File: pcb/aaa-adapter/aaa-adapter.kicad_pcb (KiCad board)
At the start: 2 copper layers, 127 x 47 mm, 3 parts

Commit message: Unchecked
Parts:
- removed REF** (x3): PinSocket_1x01_P2.54mm_Vertical, Connector_PinSocket_2.54mm:PinSocket_1x01_P2.54mm_Vertical
- added B1: ~, aaa:aaa-holder-3x1-pins, F.Cu at (15.0, 15.0)
- added J1: ~, aaa:hp-contacts, B.Cu at (32.0, 28.5)
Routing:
- net /V-: track 0.00 -> 77.5 mm
- net /V+: track 0.00 -> 77.1 mm
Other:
- board size 127 x 47 mm -> 51.5 x 38 mm
- board text added: "+"
- board text added: "3xAAA battery holder side"
- board text added: "Calculator battery well side"
- board text added: "–"

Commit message: production
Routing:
- net /V-: track 77.5 -> 78.4 mm
- net /V+: track 77.1 -> 77.9 mm
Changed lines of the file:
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@@
 		(pad "1" thru_hole circle
 			(at 2.46 7)
-			(size 1.6 1.6)
-			(drill 0.9)
+			(size 3 3)
+			(drill 1.5)
 			(layers "*.Cu" "*.Mask")
 			(remove_unused_layers no)
@@
 		(pad "2" thru_hole circle
 			(at 2.46 19)
-			(size 1.6 1.6)
-			(drill 0.9)
+			(size 3 3)
+			(drill 1.5)
 			(layers "*.Cu" "*.Mask")
 			(remove_unused_layers no)
@@
 		(pad "3" thru_hole circle
 			(at 2.5 31)
-			(size 1.6 1.6)
-			(drill 0.9)
+			(size 3 3)
+			(drill 1.5)
 			(layers "*.Cu" "*.Mask")
 			(remove_unused_layers no)
@@
 		(pad "4" thru_hole circle
 			(at 49 31)
-			(size 1.6 1.6)
-			(drill 0.9)
+			(size 3 3)
+			(drill 1.5)
 			(layers "*.Cu" "*.Mask")
 			(remove_unused_layers no)
@@
 		(pad "5" thru_hole circle
 			(at 48.96 19)
-			(size 1.6 1.6)
-			(drill 0.9)
+			(size 3 3)
+			(drill 1.5)
 			(layers "*.Cu" "*.Mask")
 			(remove_unused_layers no)
@@
 		(pad "6" thru_hole circle
 			(at 48.96 7)
-			(size 1.6 1.6)
-			(drill 0.9)
+			(size 3 3)
+			(drill 1.5)
 			(layers "*.Cu" "*.Mask")
 			(remove_unused_layers no)
@@
 	)
 	(gr_text "–"
-		(at 17.5 31.5 0)
+		(at 17.5 31 0)
 		(layer "F.SilkS")
 		(effects
@@
 	)
 	(gr_text "–"
-		(at 64 19.5 0)
+		(at 64 19 0)
 		(layer "F.SilkS")
 		(effects
@@
 	)
 	(gr_text "+"
-		(at 64 31.5 0)
+		(at 64 31 0)
 		(layer "F.SilkS")
 		(effects
@@
 	)
 	(gr_text "+"
-		(at 17.5 19.5 0)
+		(at 17.5 19 0)
 		(layer "F.SilkS")
 		(effects
@@
 	)
 	(gr_text "+"
-		(at 17.5 43.5 0)
+		(at 17.5 43 0)
 		(layer "F.SilkS")
 		(effects
@@
 	)
 	(gr_text "–"
-		(at 64 43.5 0)
-		(layer "F.SilkS")
-		(effects
-			(font
-				(size 2 2)
-				(thickness 0.25)
-			)
-		)
-	)
-	(segment
-		(start 61.5 43.5)
+		(at 64 43 0)
+		(layer "F.SilkS")
+		(effects
+			(font
+				(size 2 2)
+				(thickness 0.25)
+			)
+		)
+	)
+	(segment
+		(start 60.5 42.5)
 		(end 64 46)
 		(width 0.8)
@@
 	)
 	(segment
-		(start 61.5 24.46)
-		(end 61.5 43.5)
+		(start 63.96 22)
+		(end 60.5 25.46)
 		(width 0.8)
 		(layer "F.Cu")
@@
 	)
 	(segment
-		(start 63.96 22)
-		(end 61.5 24.46)
+		(start 60.5 25.46)
+		(end 60.5 42.5)
 		(width 0.8)
 		(layer "F.Cu")
@@
 	)
 	(segment
-		(start 19.5 44)
-		(end 17.5 46)
+		(start 20.5 25.04)
+		(end 20.5 43)
 		(width 0.8)
 		(layer "F.Cu")
@@
 	(segment
 		(start 17.46 22)
-		(end 19.5 24.04)
+		(end 20.5 25.04)
 		(width 0.8)
 		(layer "F.Cu")
@@
 	)
 	(segment
-		(start 19.5 24.04)
-		(end 19.5 44)
+		(start 20.5 43)
+		(end 17.5 46)
 		(width 0.8)
 		(layer "F.Cu")

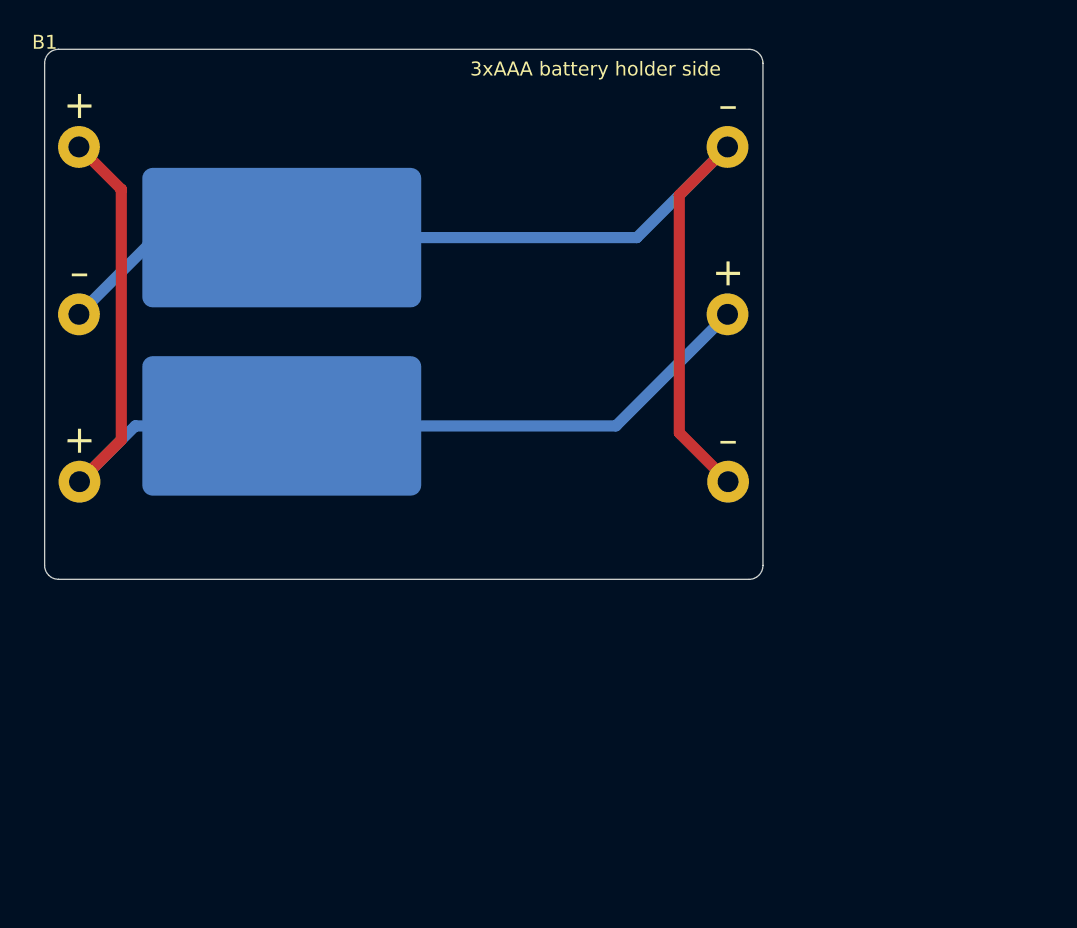
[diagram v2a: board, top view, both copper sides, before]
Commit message: Remove the need for a 3d print?
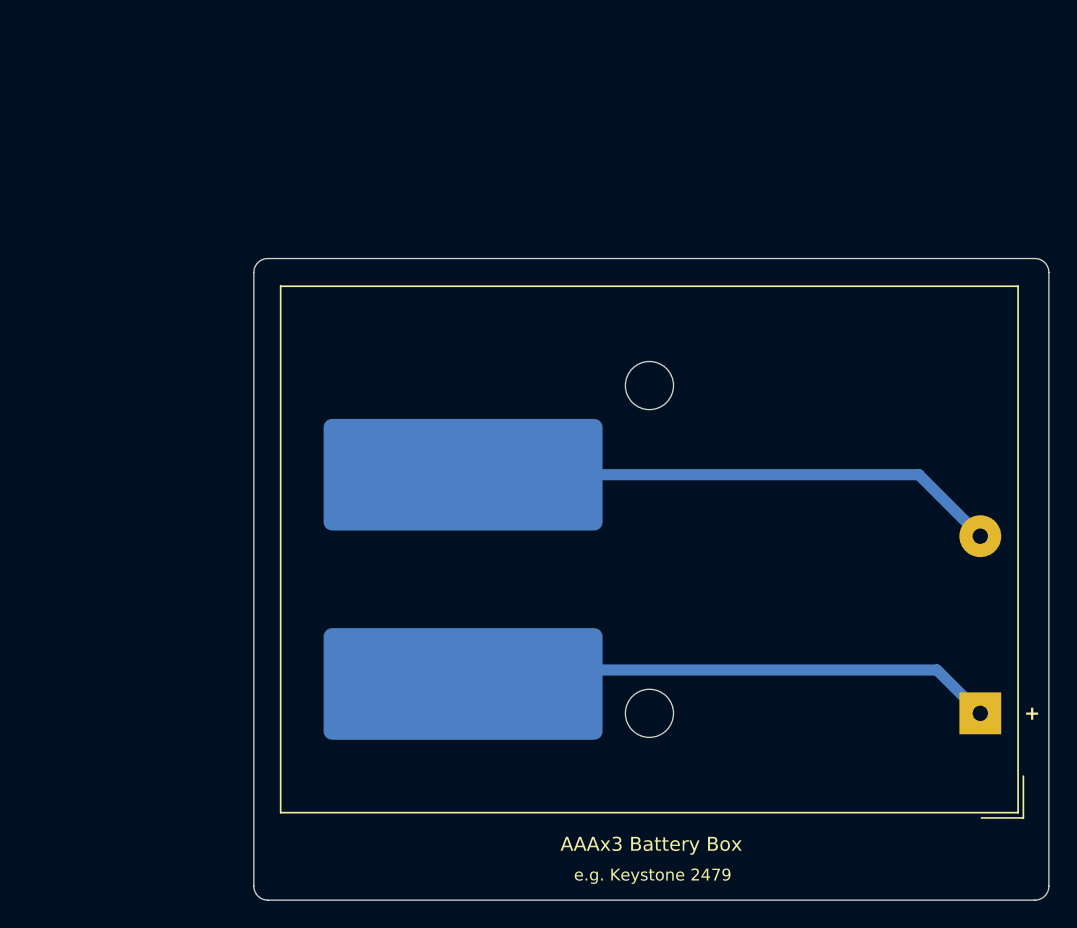
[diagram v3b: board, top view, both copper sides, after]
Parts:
- removed B1: ~, aaa:aaa-holder-3x1-pins
- added J2: AAAx3 Battery Box, Battery:BatteryHolder_Keystone_2479_3xAAA, F.Cu at (82.1, 62.6)
- moved J1 21.4 mm to (45.0, 45.5)
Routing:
- net /V-: track 78.4 -> 38.9 mm
- net /V+: track 77.9 -> 38.8 mm
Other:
- board size 51.5 x 38 mm -> 57 x 46 mm
- board text removed: "3xAAA battery holder side"
